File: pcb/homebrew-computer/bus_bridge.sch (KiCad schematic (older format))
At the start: 3 parts

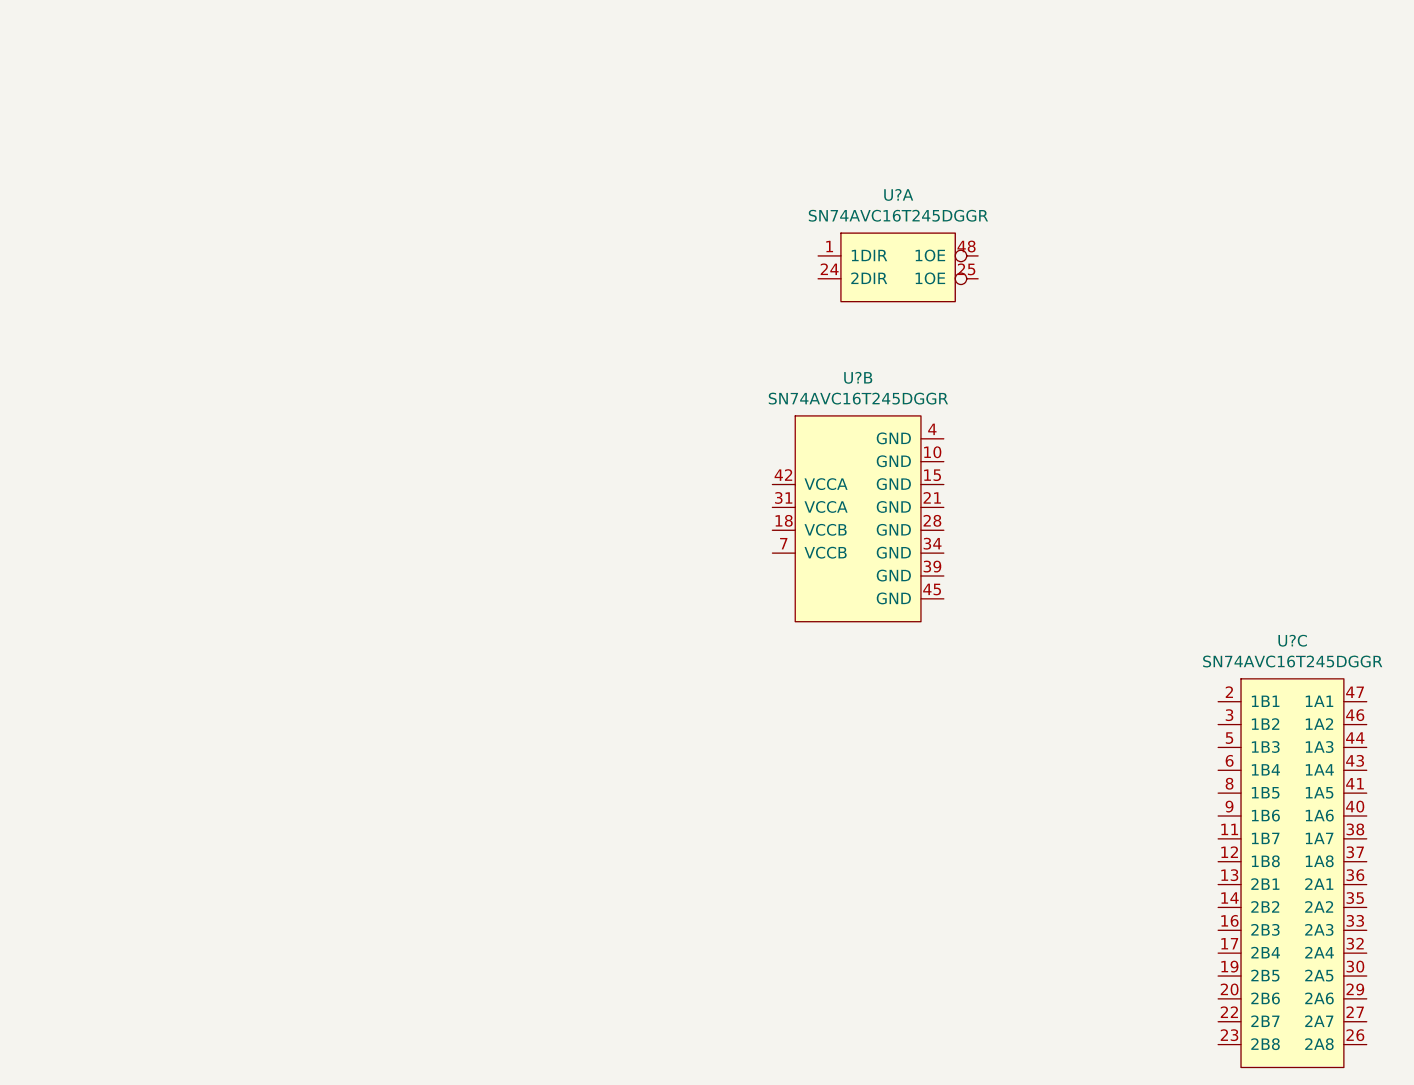
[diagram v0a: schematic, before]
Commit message: Add resistor nets for bus termination
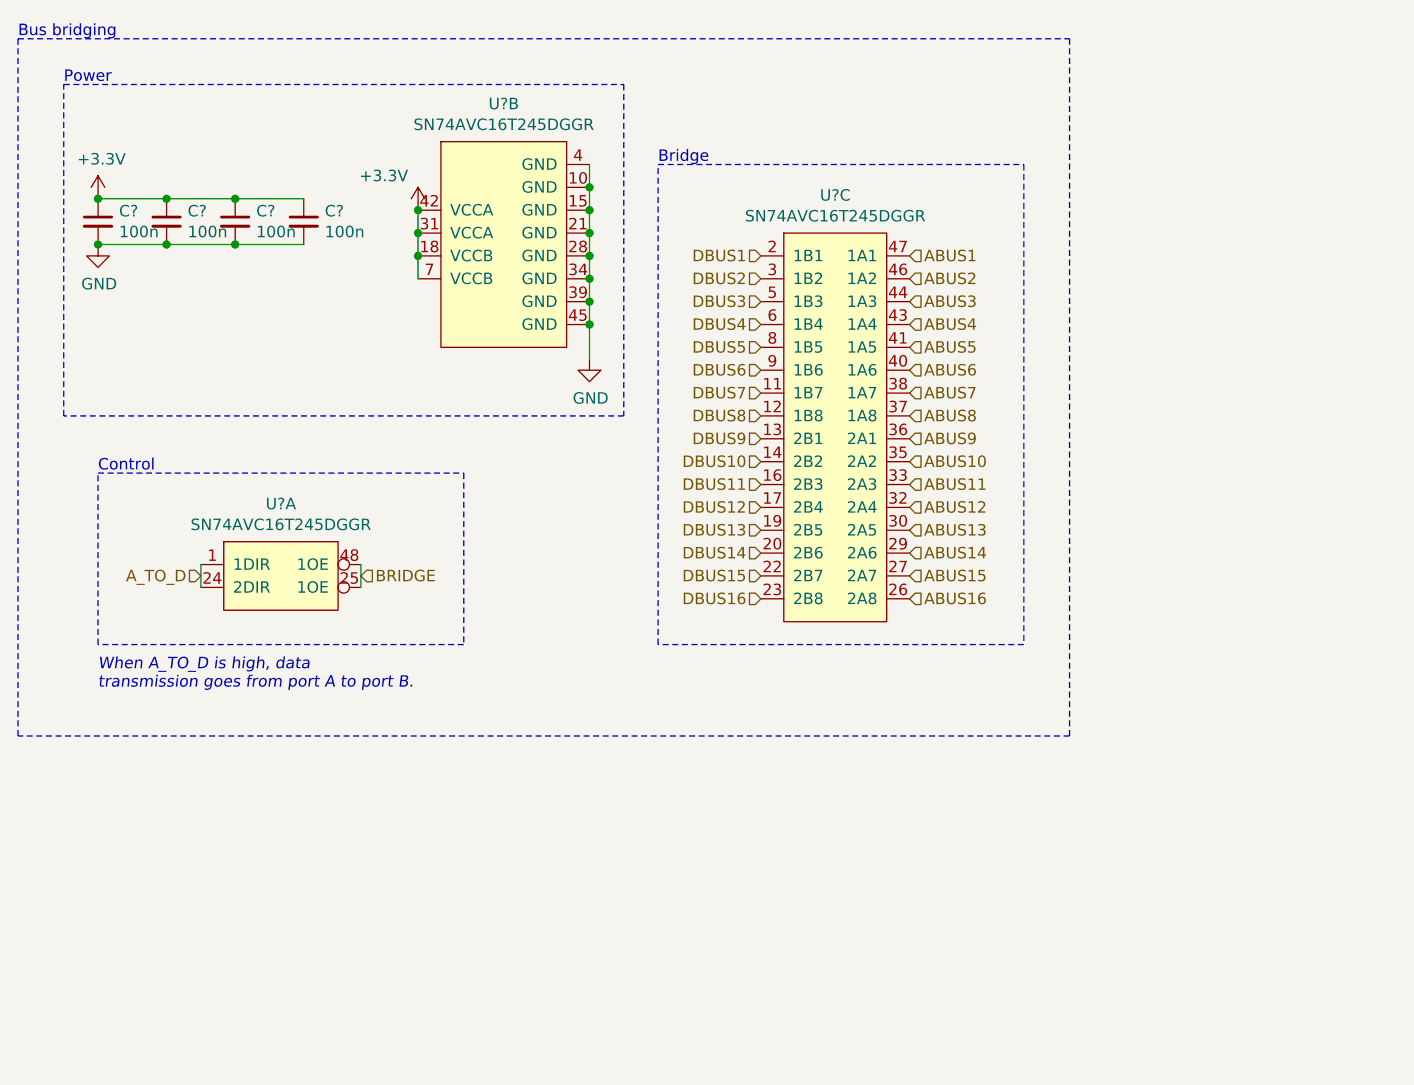
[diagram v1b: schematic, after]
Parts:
- added C? (x4): 100n, symbol Device:C_Small
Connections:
- net A_TO_D: now reaches U?.1 (1DIR)
- net A_TO_D: now also U?.24 (2DIR)
- net BRIDGE: now reaches U?.25 (1OE)
- net BRIDGE: now also U?.48 (1OE)
- net GND: now reaches U?.10 (GND)
- net GND: now also U?.15 (GND), U?.21 (GND), U?.28 (GND), U?.34 (GND), U?.39 (GND), U?.4 (GND), U?.45 (GND), C?.2, C?.2, C?.2, C?.2
- net +3V3: now reaches U?.18 (VCCB)
- net +3V3: now also U?.31 (VCCA), U?.42 (VCCA), U?.7 (VCCB), C?.1, C?.1, C?.1, C?.1
- net DBUS7: now reaches U?.11 (1B7)
- net DBUS8: now reaches U?.12 (1B8)
- net DBUS9: now reaches U?.13 (2B1)
- net DBUS10: now reaches U?.14 (2B2)
- net DBUS11: now reaches U?.16 (2B3)
- net DBUS12: now reaches U?.17 (2B4)
- net DBUS13: now reaches U?.19 (2B5)
- net DBUS1: now reaches U?.2 (1B1)
- net DBUS14: now reaches U?.20 (2B6)
- net DBUS15: now reaches U?.22 (2B7)
- net DBUS16: now reaches U?.23 (2B8)
- net ABUS16: now reaches U?.26 (2A8)
- net ABUS15: now reaches U?.27 (2A7)
- net ABUS14: now reaches U?.29 (2A6)
- net DBUS2: now reaches U?.3 (1B2)
- net ABUS13: now reaches U?.30 (2A5)
- net ABUS12: now reaches U?.32 (2A4)
- net ABUS11: now reaches U?.33 (2A3)
- net ABUS10: now reaches U?.35 (2A2)
- net ABUS9: now reaches U?.36 (2A1)
- net ABUS8: now reaches U?.37 (1A8)
- net ABUS7: now reaches U?.38 (1A7)
- net ABUS6: now reaches U?.40 (1A6)
- net ABUS5: now reaches U?.41 (1A5)
- net ABUS4: now reaches U?.43 (1A4)
- net ABUS3: now reaches U?.44 (1A3)
- net ABUS2: now reaches U?.46 (1A2)
- net ABUS1: now reaches U?.47 (1A1)
- net DBUS3: now reaches U?.5 (1B3)
- net DBUS4: now reaches U?.6 (1B4)
- net DBUS5: now reaches U?.8 (1B5)
- net DBUS6: now reaches U?.9 (1B6)
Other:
- note added: "Bridge"
- note added: "Bus bridging"
- note added: "Control"
- note added: "Power"
- note added: "When A_TO_D is high, data \ntransmission goes from port A to port B."
- moved on the sheet: U?A, U?B, U?C
